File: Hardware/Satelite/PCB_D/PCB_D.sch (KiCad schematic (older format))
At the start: 34 parts, among them J1 Conn_01x03, J2 Conector_Expansion_CanSat, J3 Conn_02x03_Odd_Even, J4 USB_B_Micro, J5 Conn_01x03, M1 Spacer, M2 Spacer, M3 Spacer, Q1 BC817, SW1 Reset Switch, U1 ATmega328P-AU, U2 CSTNE16M0V530000R0, U3 FT231XS, U4 TPD2E2U06

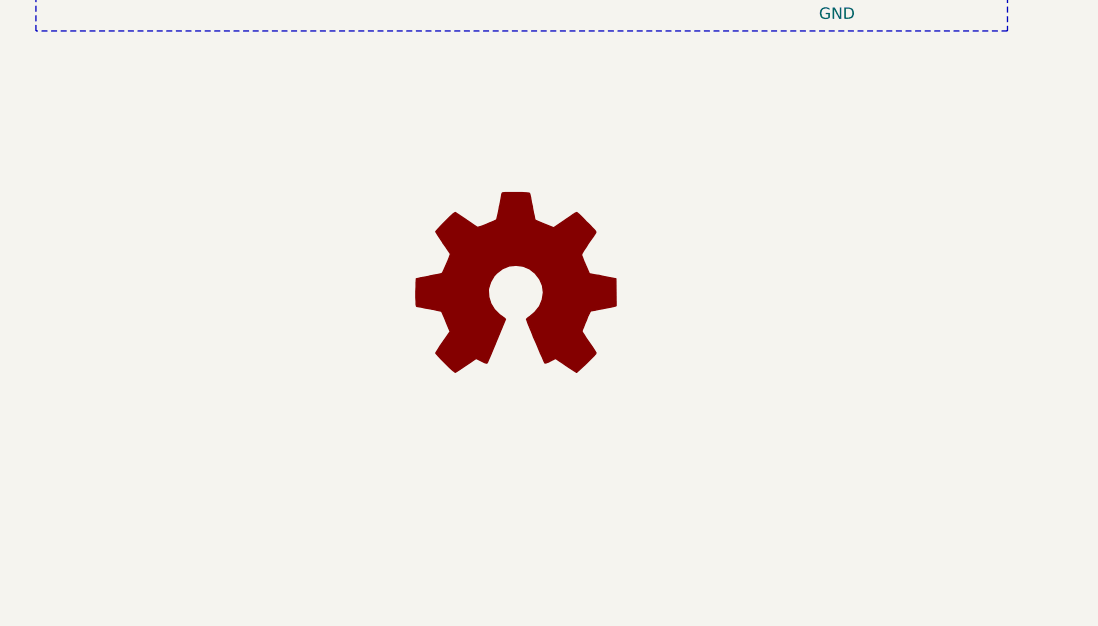
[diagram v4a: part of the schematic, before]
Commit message: Regulador de 3.3V independiente para PCB_D
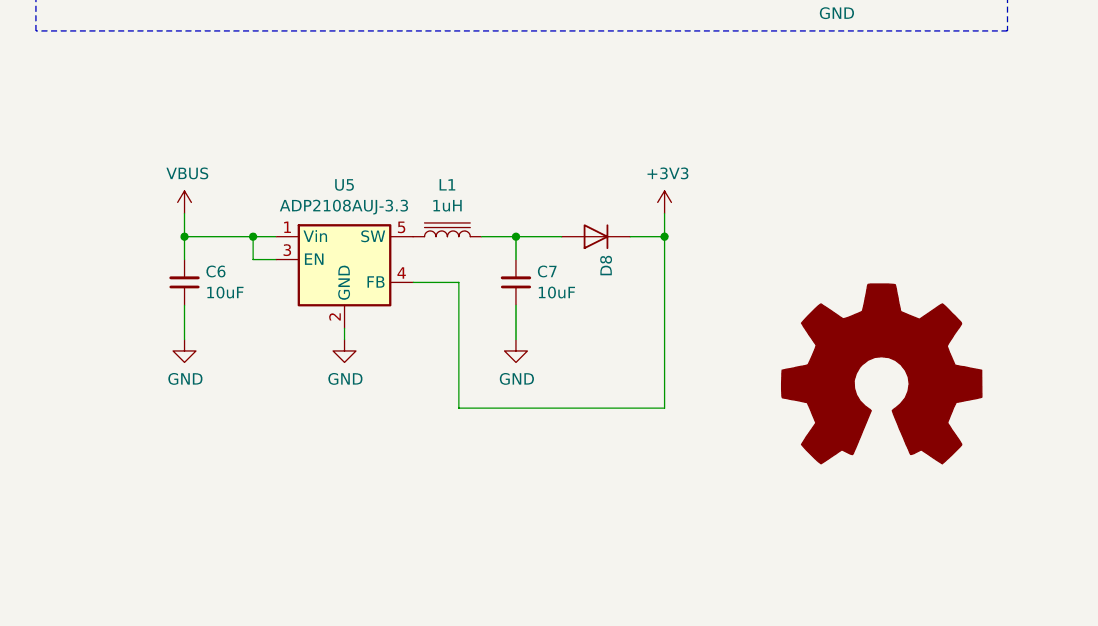
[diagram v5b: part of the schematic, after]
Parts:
- added C6, C7: 10uF, Capacitor_SMD:C_0805_2012Metric_Pad1.15x1.40mm_HandSolder, symbol Device:C_Small
- added D8: RS1A-E3/5AT, Diode_SMD:D_SMA, symbol Diode:1N4007
- added L1: 1uH, Capacitor_SMD:C_0805_2012Metric_Pad1.15x1.40mm_HandSolder, symbol Device:L_Core_Iron
- added U5: ADP2108AUJ-3.3, Package_TO_SOT_SMD:TSOT-23-5, symbol Regulator_Switching:ADP2108AUJ-3.3
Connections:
- wire segments 156 -> 174
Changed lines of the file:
@@
 L Graphic:Logo_Open_Hardware_Large #LOGO1
 U 1 1 5C3319FC
-P 8750 5500
-F 0 "#LOGO1" H 8750 6000 50  0001 C CNN
-F 1 "Logo_Open_Hardware_Large" H 8750 5100 50  0001 C CNN
-F 2 "" H 8750 5500 50  0001 C CNN
-F 3 "~" H 8750 5500 50  0001 C CNN
-	1    8750 5500
+P 10350 5900
+F 0 "#LOGO1" H 10350 6400 50  0001 C CNN
+F 1 "Logo_Open_Hardware_Large" H 10350 5500 50  0001 C CNN
+F 2 "" H 10350 5900 50  0001 C CNN
+F 3 "~" H 10350 5900 50  0001 C CNN
+	1    10350 5900
 	1    0    0    -1
 $EndComp
@@
 Text Label 4250 6900 0    50   ~ 0
 TX_SUP
+$Comp
+L Regulator_Switching:ADP2108AUJ-3.3 U5
+U 1 1 5D12D70C
+P 8000 5350
+F 0 "U5" H 8000 5675 50  0000 C CNN
+F 1 "ADP2108AUJ-3.3" H 8000 5584 50  0000 C CNN
+F 2 "Package_TO_SOT_SMD:TSOT-23-5" H 8050 5100 50  0001 L CNN
+F 3 "https://www.analog.com/media/en/technical-documentation/data-sheets/ADP2108.pdf" H 7750 5000 50  0001 C CNN
+F 4 "ADP2108AUJZ-3.3-R7" H 8000 5350 50  0001 C CNN "Manufacturer Part Number"
+	1    8000 5350
+	1    0    0    -1
+$EndComp
+$Comp
+L Device:C_Small C6
+U 1 1 5D12EDB8
+P 7300 5450
+F 0 "C6" H 7208 5404 50  0000 R CNN
+F 1 "10uF" H 7208 5496 50  0000 R CNN
+F 2 "Capacitor_SMD:C_0805_2012Metric_Pad1.15x1.40mm_HandSolder" H 7300 5450 50  0001 C CNN
+F 3 "~" H 7300 5450 50  0001 C CNN
+F 4 "C2012X7R1A106M125AC" H 7300 5450 50  0001 C CNN "Manufacturer Part Number"
+	1    7300 5450
+	-1   0    0    1
+$EndComp
+$Comp
+L Device:C_Small C7
+U 1 1 5D12FAD1
+P 8750 5450
+F 0 "C7" H 8658 5404 50  0000 R CNN
+F 1 "10uF" H 8658 5496 50  0000 R CNN
+F 2 "Capacitor_SMD:C_0805_2012Metric_Pad1.15x1.40mm_HandSolder" H 8750 5450 50  0001 C CNN
+F 3 "~" H 8750 5450 50  0001 C CNN
+F 4 "C2012X7R1A106M125AC" H 8750 5450 50  0001 C CNN "Manufacturer Part Number"
+	1    8750 5450
+	-1   0    0    1
+$EndComp
+$Comp
+L Device:L_Core_Iron L1
+U 1 1 5D130B73
+P 8450 5250
+F 0 "L1" V 8675 5250 50  0000 C CNN
+F 1 "1uH" V 8584 5250 50  0000 C CNN
+F 2 "Capacitor_SMD:C_0805_2012Metric_Pad1.15x1.40mm_HandSolder" H 8450 5250 50  0001 C CNN
+F 3 "~" H 8450 5250 50  0001 C CNN
+F 4 "LQM21PN1R0MC0D" V 8450 5250 50  0001 C CNN "Manufacturer Part Number"
+	1    8450 5250
+	0    -1   -1   0
+$EndComp
+Wire Wire Line
+	7700 5350 7600 5350
+Wire Wire Line
+	7600 5350 7600 5250
+Wire Wire Line
+	7600 5250 7700 5250
+$Comp
+L power:GND #PWR028
+U 1 1 5D13C356
+P 8000 5700
+F 0 "#PWR028" H 8000 5450 50  0001 C CNN
+F 1 "GND" H 8004 5526 50  0000 C CNN
+F 2 "" H 8000 5700 50  0001 C CNN
+F 3 "" H 8000 5700 50  0001 C CNN
+	1    8000 5700
+	1    0    0    -1
+$EndComp
+Wire Wire Line
+	7600 5250 7300 5250
+Wire Wire Line
+	7300 5250 7300 5350
+Connection ~ 7600 5250
+$Comp
+L power:GND #PWR027
+U 1 1 5D14502C
+P 7300 5700
+F 0 "#PWR027" H 7300 5450 50  0001 C CNN
+F 1 "GND" H 7304 5526 50  0000 C CNN
+F 2 "" H 7300 5700 50  0001 C CNN
+F 3 "" H 7300 5700 50  0001 C CNN
+	1    7300 5700
+	1    0    0    -1
+$EndComp
+Wire Wire Line
+	7300 5700 7300 5550
+Wire Wire Line
+	8000 5650 8000 5700
+Wire Wire Line
+	8750 5350 8750 5250
+Wire Wire Line
+	8750 5250 8600 5250
+$Comp
+L power:GND #PWR029
+U 1 1 5D168122
+P 8750 5700
+F 0 "#PWR029" H 8750 5450 50  0001 C CNN
+F 1 "GND" H 8754 5526 50  0000 C CNN
+F 2 "" H 8750 5700 50  0001 C CNN
+F 3 "" H 8750 5700 50  0001 C CNN
+	1    8750 5700
+	1    0    0    -1
+$EndComp
+Wire Wire Line
+	8750 5700 8750 5550
+$Comp
+L Diode:1N4007 D8
+U 1 1 5D17106F
+P 9100 5250
+F 0 "D8" V 9054 5329 50  0000 L CNN
+F 1 "RS1A-E3/5AT" V 9146 5329 50  0001 L CNN
+F 2 "Diode_SMD:D_SMA" H 9100 5075 50  0001 C CNN
+F 3 "http://www.vishay.com/docs/88503/1n4001.pdf" H 9100 5250 50  0001 C CNN
+F 4 "RS1A-E3/5AT" V 9100 5250 50  0001 C CNN "Manufacturer Part Number"
+	1    9100 5250
+	-1   0    0    1
+$EndComp
+Wire Wire Line
+	8950 5250 8750 5250
+Connection ~ 8750 5250
+Wire Wire Line
+	8300 5450 8500 5450
+Wire Wire Line
+	8500 5450 8500 6000
+Wire Wire Line
+	8500 6000 9400 6000
+Wire Wire Line
+	9400 6000 9400 5250
+Wire Wire Line
+	9400 5250 9250 5250
+$Comp
+L power:+3V3 #PWR030
+U 1 1 5D185125
+P 9400 5150
+F 0 "#PWR030" H 9400 5000 50  0001 C CNN
+F 1 "+3V3" H 9414 5325 50  0000 C CNN
+F 2 "" H 9400 5150 50  0001 C CNN
+F 3 "" H 9400 5150 50  0001 C CNN
+	1    9400 5150
+	1    0    0    -1
+$EndComp
+Wire Wire Line
+	9400 5150 9400 5250
+Connection ~ 9400 5250
+$Comp
+L power:VBUS #PWR026
+U 1 1 5D19B571
+P 7300 5150
+F 0 "#PWR026" H 7300 5000 50  0001 C CNN
+F 1 "VBUS" H 7314 5325 50  0000 C CNN
+F 2 "" H 7300 5150 50  0001 C CNN
+F 3 "" H 7300 5150 50  0001 C CNN
+	1    7300 5150
+	1    0    0    -1
+$EndComp
+Wire Wire Line
+	7300 5150 7300 5250
+Connection ~ 7300 5250
 $EndSCHEMATC
